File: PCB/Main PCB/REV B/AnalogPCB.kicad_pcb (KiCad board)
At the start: 4 copper layers, 95 x 140 mm, 60 parts, among them J1 DF12NB_4.0_-20DP-0.5V_51_, J2 393570002, J3 393570002, J4 393570002, J5 393570002, J6 Conn_01x03_Female, Q1 2N7002, Q2 2N7002, Q3 2N7002, U1 ALDP105W, U2 ALDP105W, U3 ALDP105W, U4 TS5A23159DGS

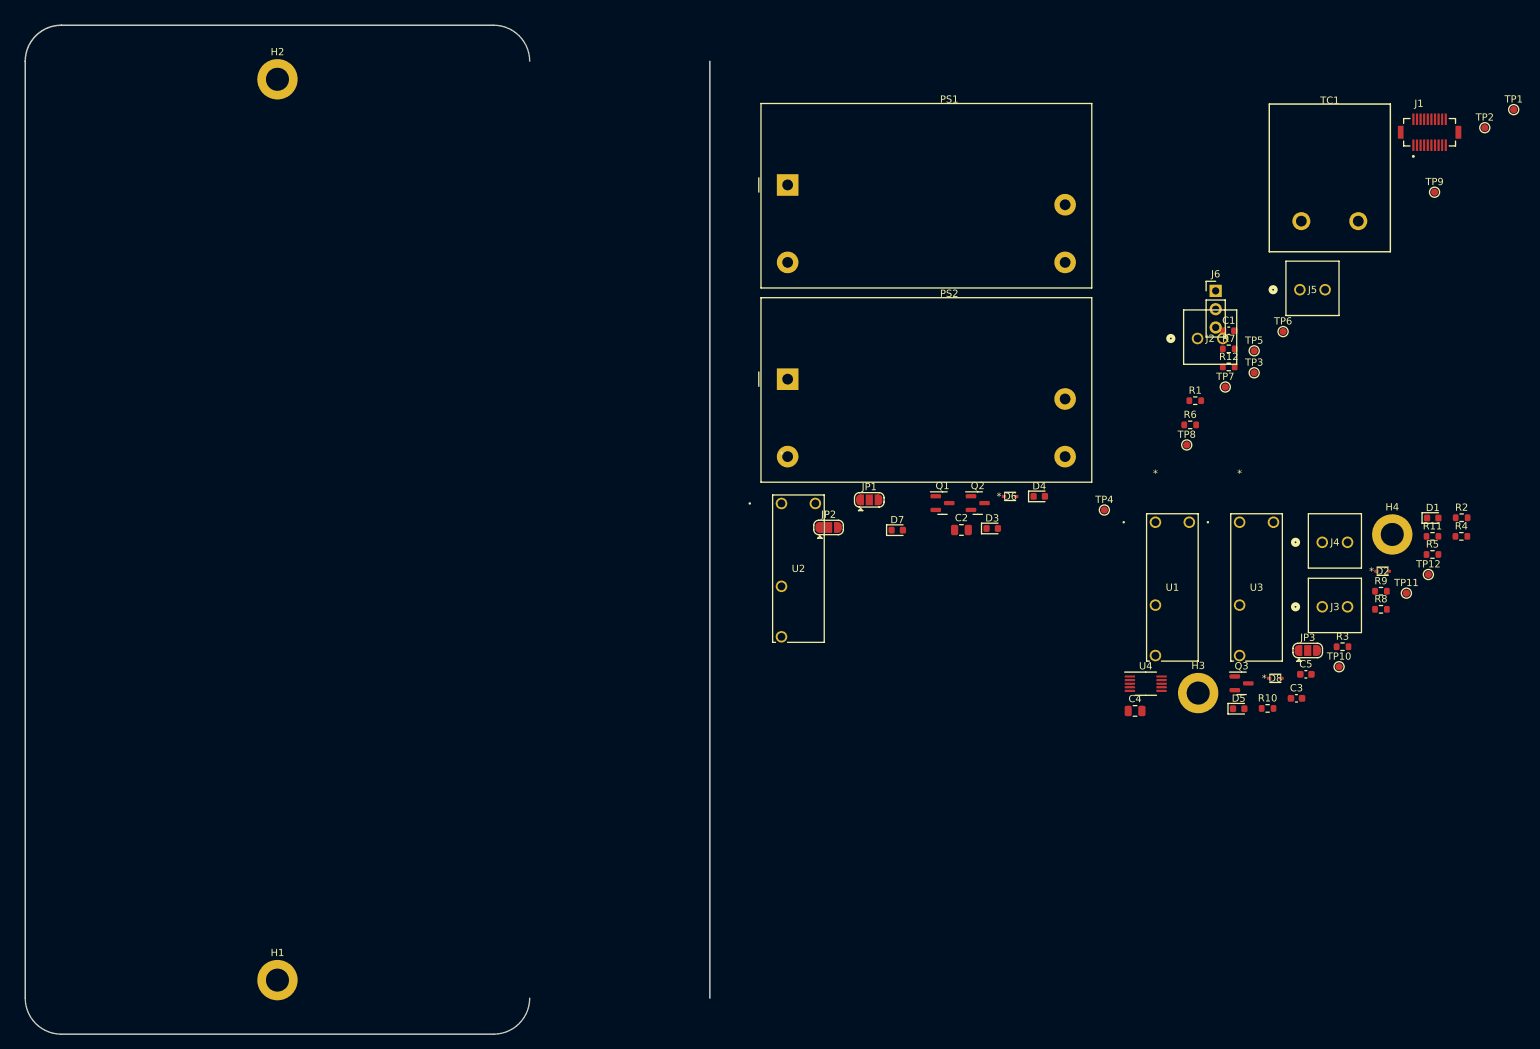
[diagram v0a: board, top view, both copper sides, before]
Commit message: PCB - Rough Analog Layout
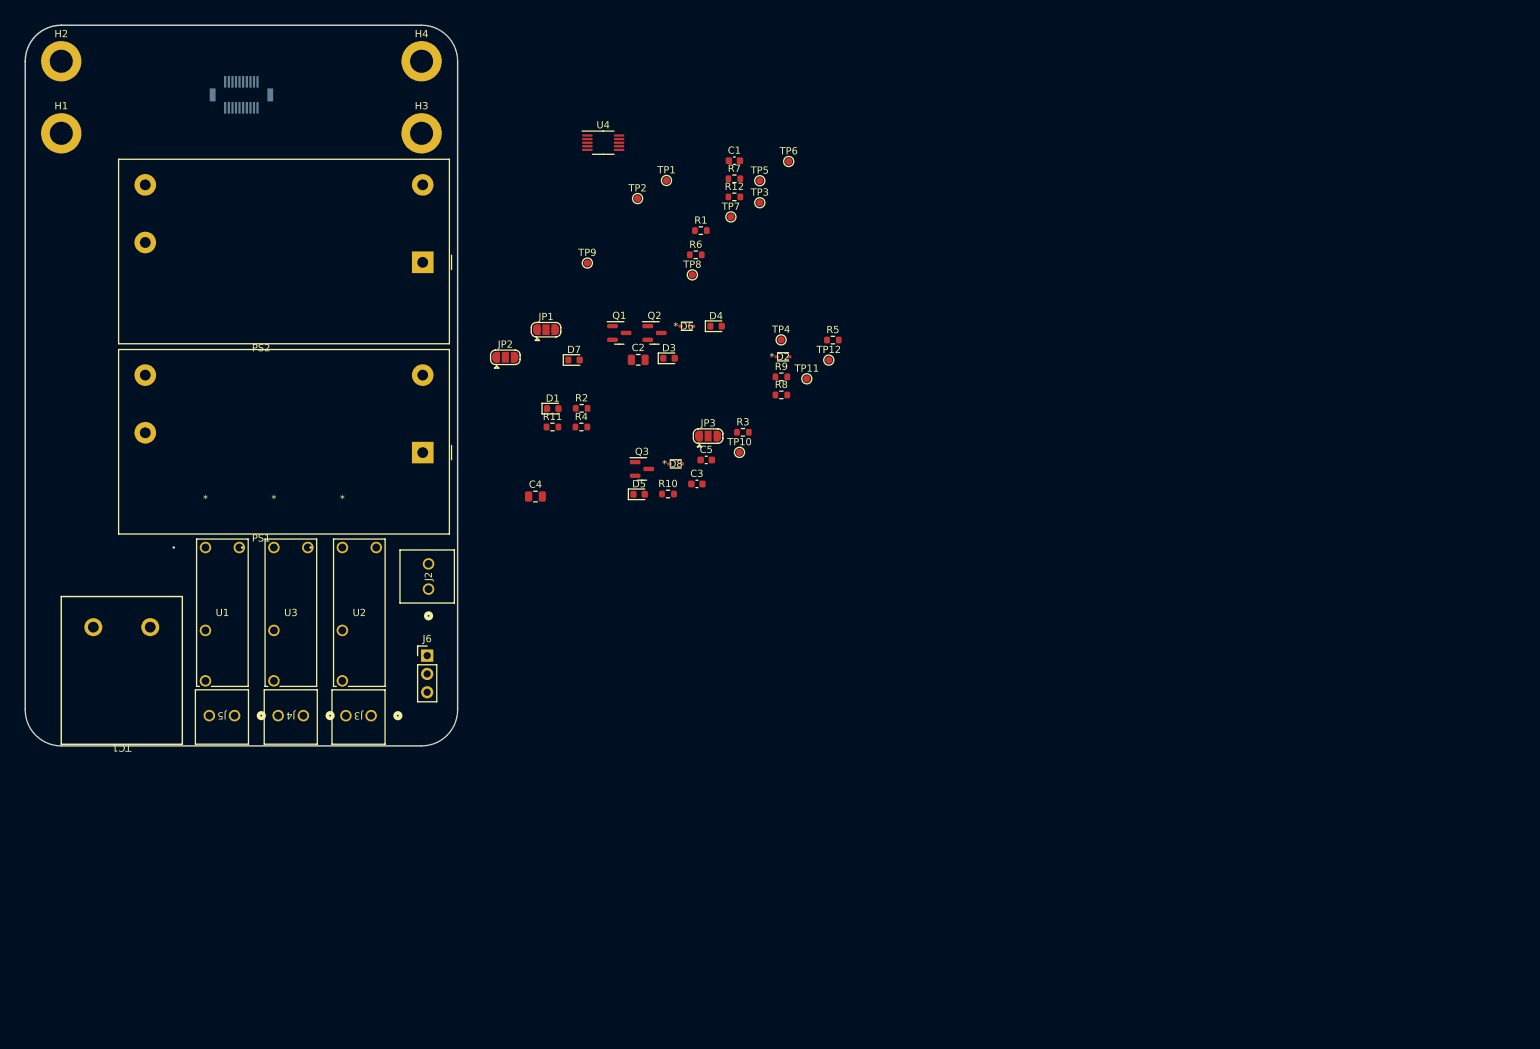
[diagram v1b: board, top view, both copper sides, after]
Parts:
- J1: moved to B.Cu
- moved TC1 189.7 mm to (63.4, 149.8), turned to 180 degrees
- moved J1 165.0 mm to (80.0, 59.7), turned to 180 degrees
- moved J5 159.2 mm to (79.0, 145.8), turned to 180 degrees
- moved H4 149.8 mm to (105.0, 55.0)
- moved J4 143.4 mm to (88.6, 145.8), turned to 180 degrees
- moved U3 134.0 mm to (84.5, 122.5)
- moved J3 132.8 mm to (98.0, 145.8), turned to 180 degrees
- moved H3 132.8 mm to (105.0, 65.0)
- moved U1 131.9 mm to (75.0, 122.5)
- moved R11 123.0 mm to (123.2, 105.8)
- moved D1 123.0 mm to (123.2, 103.2)
- moved R2 123.0 mm to (127.2, 103.2)
- moved R4 123.0 mm to (127.2, 105.8)
- moved H1 121.3 mm to (55.0, 65.0)
- moved J6 120.6 mm to (105.8, 137.5)
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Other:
- board size 95 x 140 mm -> 60 x 100 mm

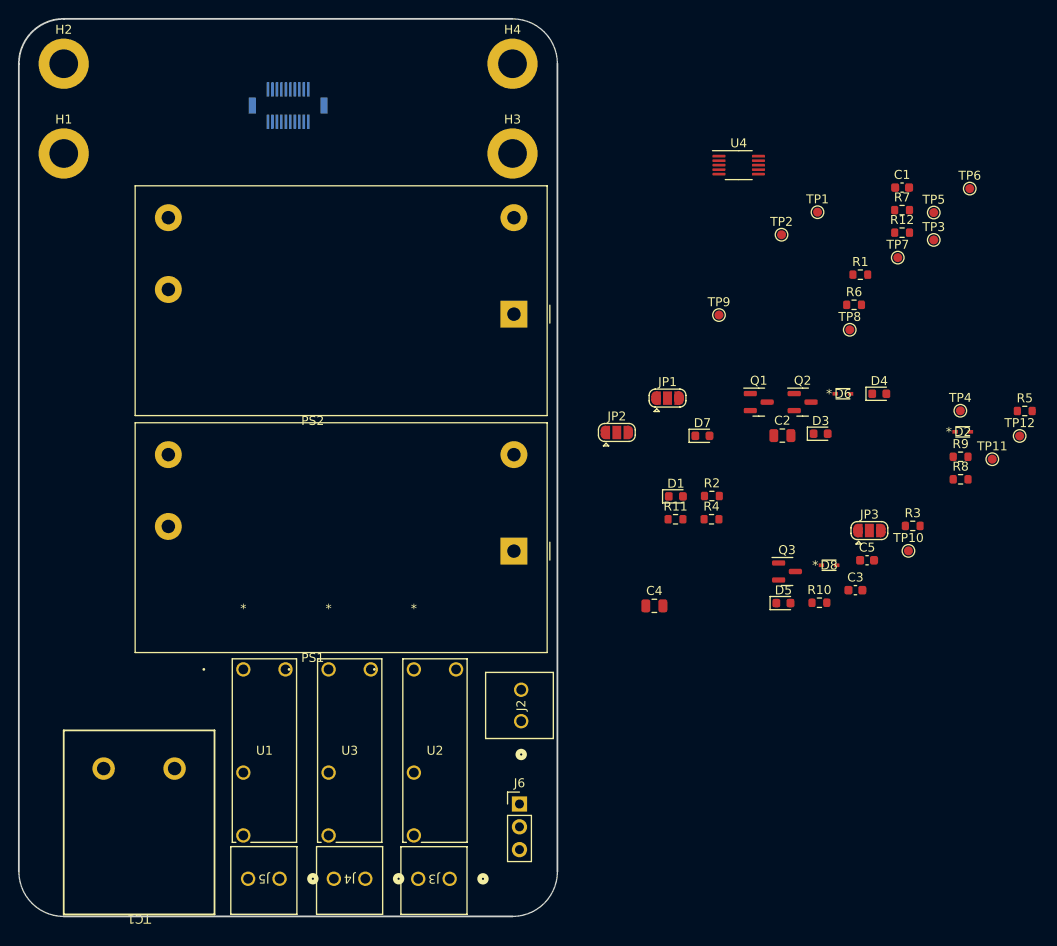
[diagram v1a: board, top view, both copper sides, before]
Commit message: PCB - Rough Analog Layout and probe jack change to RTD
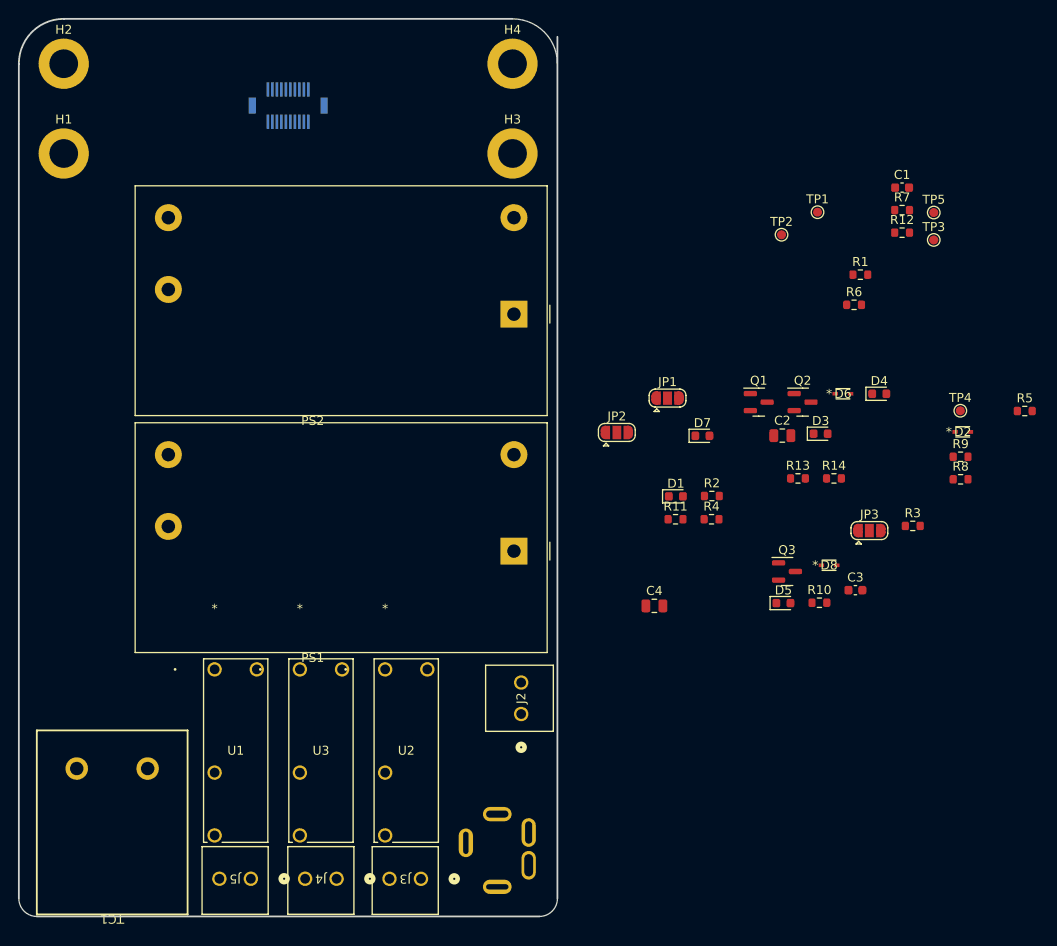
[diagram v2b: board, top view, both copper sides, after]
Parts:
- removed C5: 0.1uF 50V X7R 0603, Capacitor_SMD:C_0603_1608Metric
- removed TP10, TP11, TP12, TP6, TP7, TP8, TP9: TP, TestPoint:TestPoint_Pad_D1.0mm
- removed U4: TS5A23159DGS, Package_SO:VSSOP-10_3x3mm_P0.5mm
- added R13: 1kOhm 1% 0603, Resistor_SMD:R_0603_1608Metric, F.Cu at (136.8, 101.2)
- added R14: 1kOhm 1% 0603, Resistor_SMD:R_0603_1608Metric, F.Cu at (140.8, 101.2)
- J6: value Conn_01x03_Female -> SJ3-35053D; footprint Connector_PinHeader_2.54mm:PinHeader_1x03_P2.54mm_Vertical -> Customs Smoker:SAMESKY_SJ3-35053D; moved to B.Cu
- R12: value 10K 1% 0603 -> 1kOhm 1% 0603
- moved J6 7.38 mm to (99.8, 141.8), turned to 180 degrees
- moved J3 3.20 mm to (94.8, 145.8)
- moved J5 3.20 mm to (75.8, 145.8)
- moved U1 3.20 mm to (71.8, 122.5)
- moved U2 3.20 mm to (90.8, 122.5)
- moved U3 3.20 mm to (81.3, 122.5)
- moved J4 3.20 mm to (85.4, 145.8)
- moved TC1 3.00 mm to (60.4, 149.8)
- moved J2 0.80 mm to (106.0, 127.4)
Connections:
- net /TipSwitchProbe2 renamed /MeatProbeRing
- J1 pad 18: /MUX_OUT_- -> /Probe1-
- J1 pad 19: /MUX_OUT_+ -> /Probe1+
- J1 pad 20: /IO2 -> /MuxSignal
- J6 pad 1: /Probe2- -> /MeatProbeSleeve
- J6 pad 2: /Probe2+ -> /MeatProbeTip
- R12 pad 1: /IO2 -> +3.3VA
- R12 pad 2: GND -> /MeatProbe+
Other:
- outline, holes or cut-outs redrawn

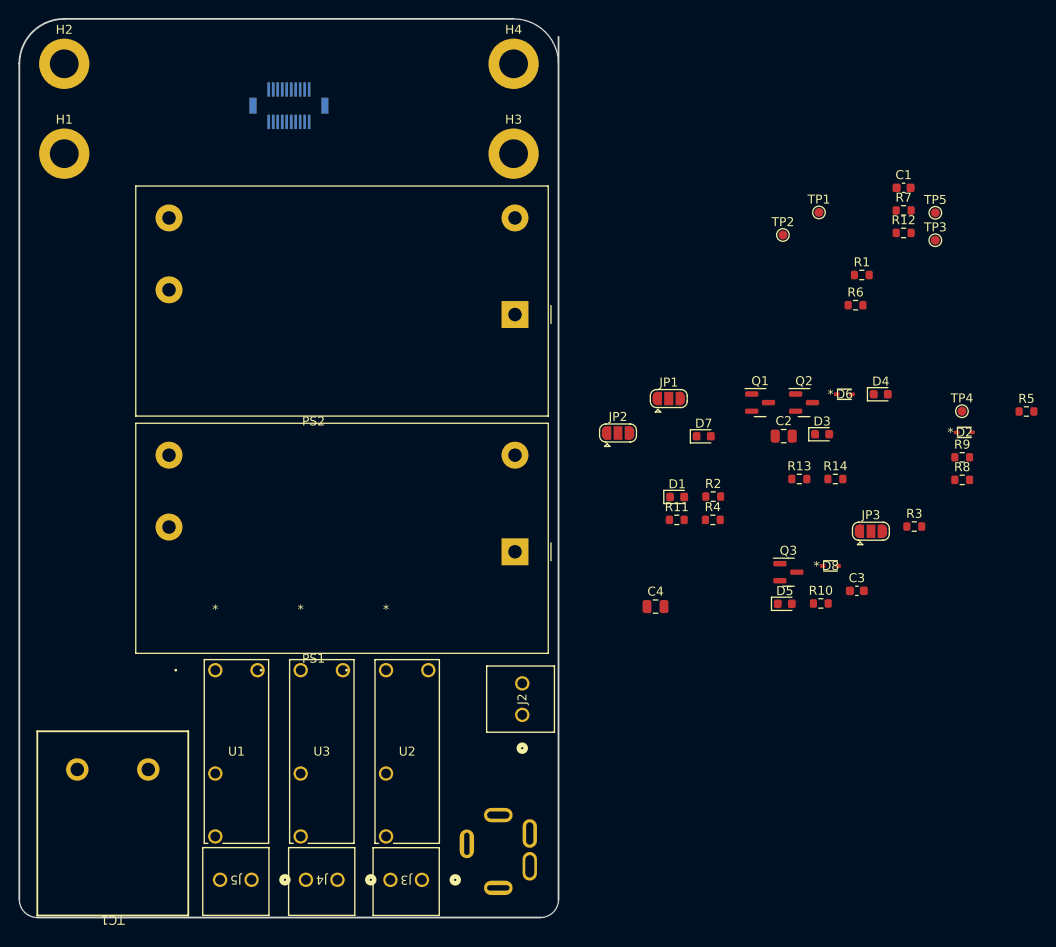
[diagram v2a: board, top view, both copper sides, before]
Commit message: PCB - Lay out analog led and power filtering
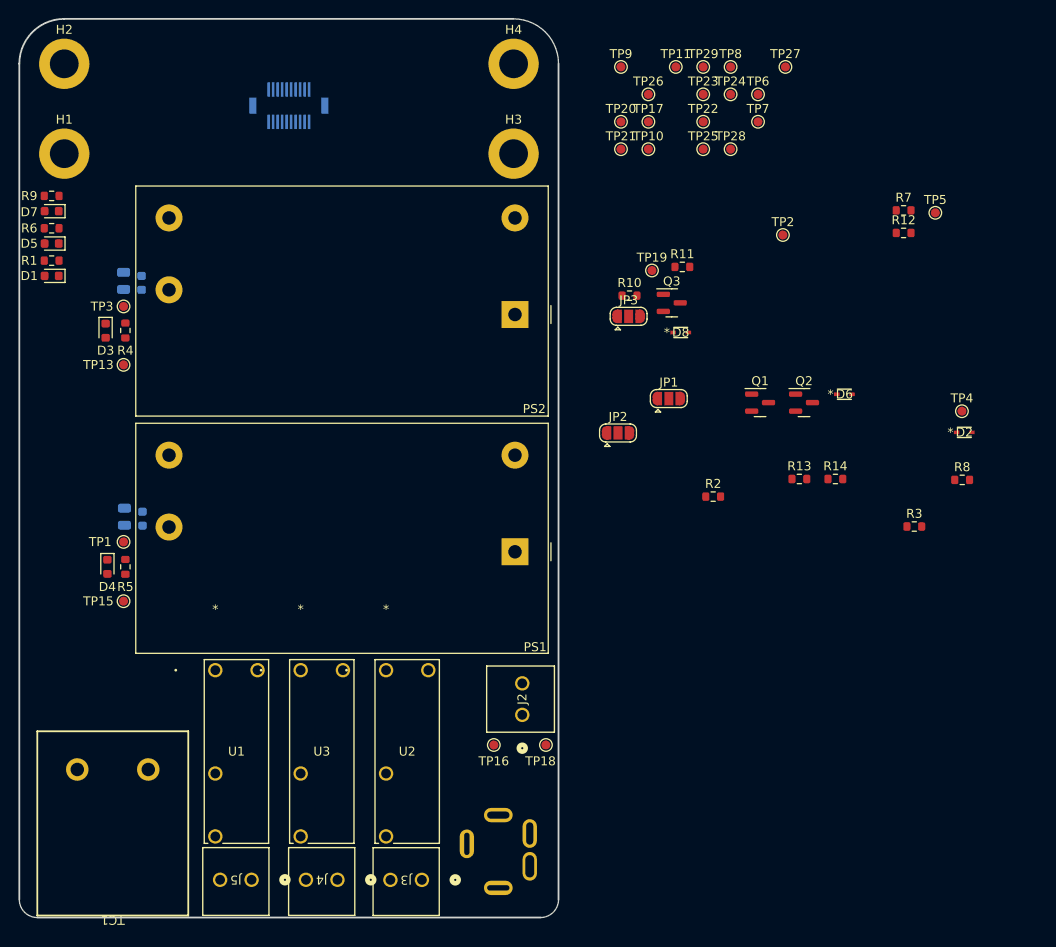
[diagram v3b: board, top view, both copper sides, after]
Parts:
- added TP10: TP, TestPoint:TestPoint_Pad_D1.0mm, F.Cu at (120.0, 64.5)
- added TP11: TP, TestPoint:TestPoint_Pad_D1.0mm, F.Cu at (123.0, 55.4)
- added TP13: TP, TestPoint:TestPoint_Pad_D1.0mm, F.Cu at (61.6, 88.5)
- added TP15: TP, TestPoint:TestPoint_Pad_D1.0mm, F.Cu at (61.6, 114.8)
- added TP16: TP, TestPoint:TestPoint_Pad_D1.0mm, F.Cu at (102.8, 130.8)
- added TP17: TP, TestPoint:TestPoint_Pad_D1.0mm, F.Cu at (120.0, 61.5)
- added TP18: TP, TestPoint:TestPoint_Pad_D1.0mm, F.Cu at (108.6, 130.8)
- added TP19: TP, TestPoint:TestPoint_Pad_D1.0mm, F.Cu at (120.4, 78.0)
- added TP20: TP, TestPoint:TestPoint_Pad_D1.0mm, F.Cu at (117.0, 61.5)
- added TP21: TP, TestPoint:TestPoint_Pad_D1.0mm, F.Cu at (117.0, 64.5)
- added TP22: TP, TestPoint:TestPoint_Pad_D1.0mm, F.Cu at (126.1, 61.5)
- added TP23: TP, TestPoint:TestPoint_Pad_D1.0mm, F.Cu at (126.1, 58.4)
- added TP24: TP, TestPoint:TestPoint_Pad_D1.0mm, F.Cu at (129.2, 58.4)
- added TP25: TP, TestPoint:TestPoint_Pad_D1.0mm, F.Cu at (126.1, 64.5)
- added TP26: TP, TestPoint:TestPoint_Pad_D1.0mm, F.Cu at (120.0, 58.4)
- added TP27: TP, TestPoint:TestPoint_Pad_D1.0mm, F.Cu at (135.2, 55.4)
- added TP28: TP, TestPoint:TestPoint_Pad_D1.0mm, F.Cu at (129.2, 64.5)
- added TP29: TP, TestPoint:TestPoint_Pad_D1.0mm, F.Cu at (126.1, 55.4)
- added TP6: TP, TestPoint:TestPoint_Pad_D1.0mm, F.Cu at (132.2, 58.4)
- added TP7: TP, TestPoint:TestPoint_Pad_D1.0mm, F.Cu at (132.2, 61.5)
- added TP8: TP, TestPoint:TestPoint_Pad_D1.0mm, F.Cu at (129.2, 55.4)
- added TP9: TP, TestPoint:TestPoint_Pad_D1.0mm, F.Cu at (117.0, 55.4)
- C1, C2, C3, C4: moved to B.Cu
- moved R9 105.4 mm to (53.6, 69.7), turned to 180 degrees
- moved R5 101.7 mm to (61.8, 111.0), turned to -90 degrees
- moved C1 92.4 mm to (63.7, 105.6), turned to -90 degrees
- moved D5 90.9 mm to (53.6, 75.0), turned to 180 degrees
- moved TP3 90.6 mm to (61.6, 82.0)
- moved R1 90.2 mm to (53.6, 76.9), turned to 180 degrees
- moved R6 89.9 mm to (53.6, 73.3), turned to 180 degrees
- moved D4 88.2 mm to (59.8, 111.0), turned to -90 degrees
- moved C3 86.7 mm to (63.6, 79.4), turned to -90 degrees
- moved TP1 85.6 mm to (61.6, 108.2)
- moved D3 80.6 mm to (59.6, 84.7), turned to -90 degrees
- moved D7 76.8 mm to (53.6, 71.4), turned to 180 degrees
- moved C2 73.9 mm to (61.7, 105.4), turned to 90 degrees
- moved D1 73.8 mm to (53.6, 78.6), turned to 180 degrees
- moved C4 69.4 mm to (61.6, 79.2), turned to 90 degrees
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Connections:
- J1 pad 13: +5V -> /Probe1+
- J1 pad 14: GND -> /Probe1-
- J1 pad 18: /Probe1- -> /MeatProbeSleeve
- J1 pad 19: /Probe1+ -> /MeatProbeRing
- J1 pad 20: /MuxSignal -> /MeatProbeTip
- TP4 pad 1: /Opto_Ignitor -> /Probe1+
- TP5 pad 1: /Opto_Fan -> /Opto_Auger
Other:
- outline, holes or cut-outs redrawn
